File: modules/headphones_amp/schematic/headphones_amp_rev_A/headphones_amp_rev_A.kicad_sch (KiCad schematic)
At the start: 94 parts, among them J1 AudioJack3_SwitchTR, J2 AudioJack3_SwitchTR, Q1 BC140, Q10 BC548, Q11 BC548, Q12 BC140, Q13 BC160, Q14 BC548, Q15 BC557, Q16 BC548, Q2 BC160, Q3 BC548, Q4 BC557, Q5 BC548, Q6 BC548, Q7 BC548, Q8 BC557, Q9 BC557, SW1 SW_SPDT, SW2 SW_SPDT

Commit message: added draft footprint for the Wurth Connector
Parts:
- added C11, C12: 100pF, Capacitor_THT:C_Rect_L7.0mm_W2.0mm_P5.00mm, symbol Device:C
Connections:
- net at Q1.3 (C), R3.2: now also C11.2
- net at Q2.2 (B), Q5.1 (C), Q7.3 (E)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: now also C12.1
- net at Q2.3 (C), R4.1, R6.1: now also C12.2
- net at Q1.2 (B), Q7.1 (C), R14.1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: now also C11.1
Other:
- moved on the sheet: H1, H2, H3, H4

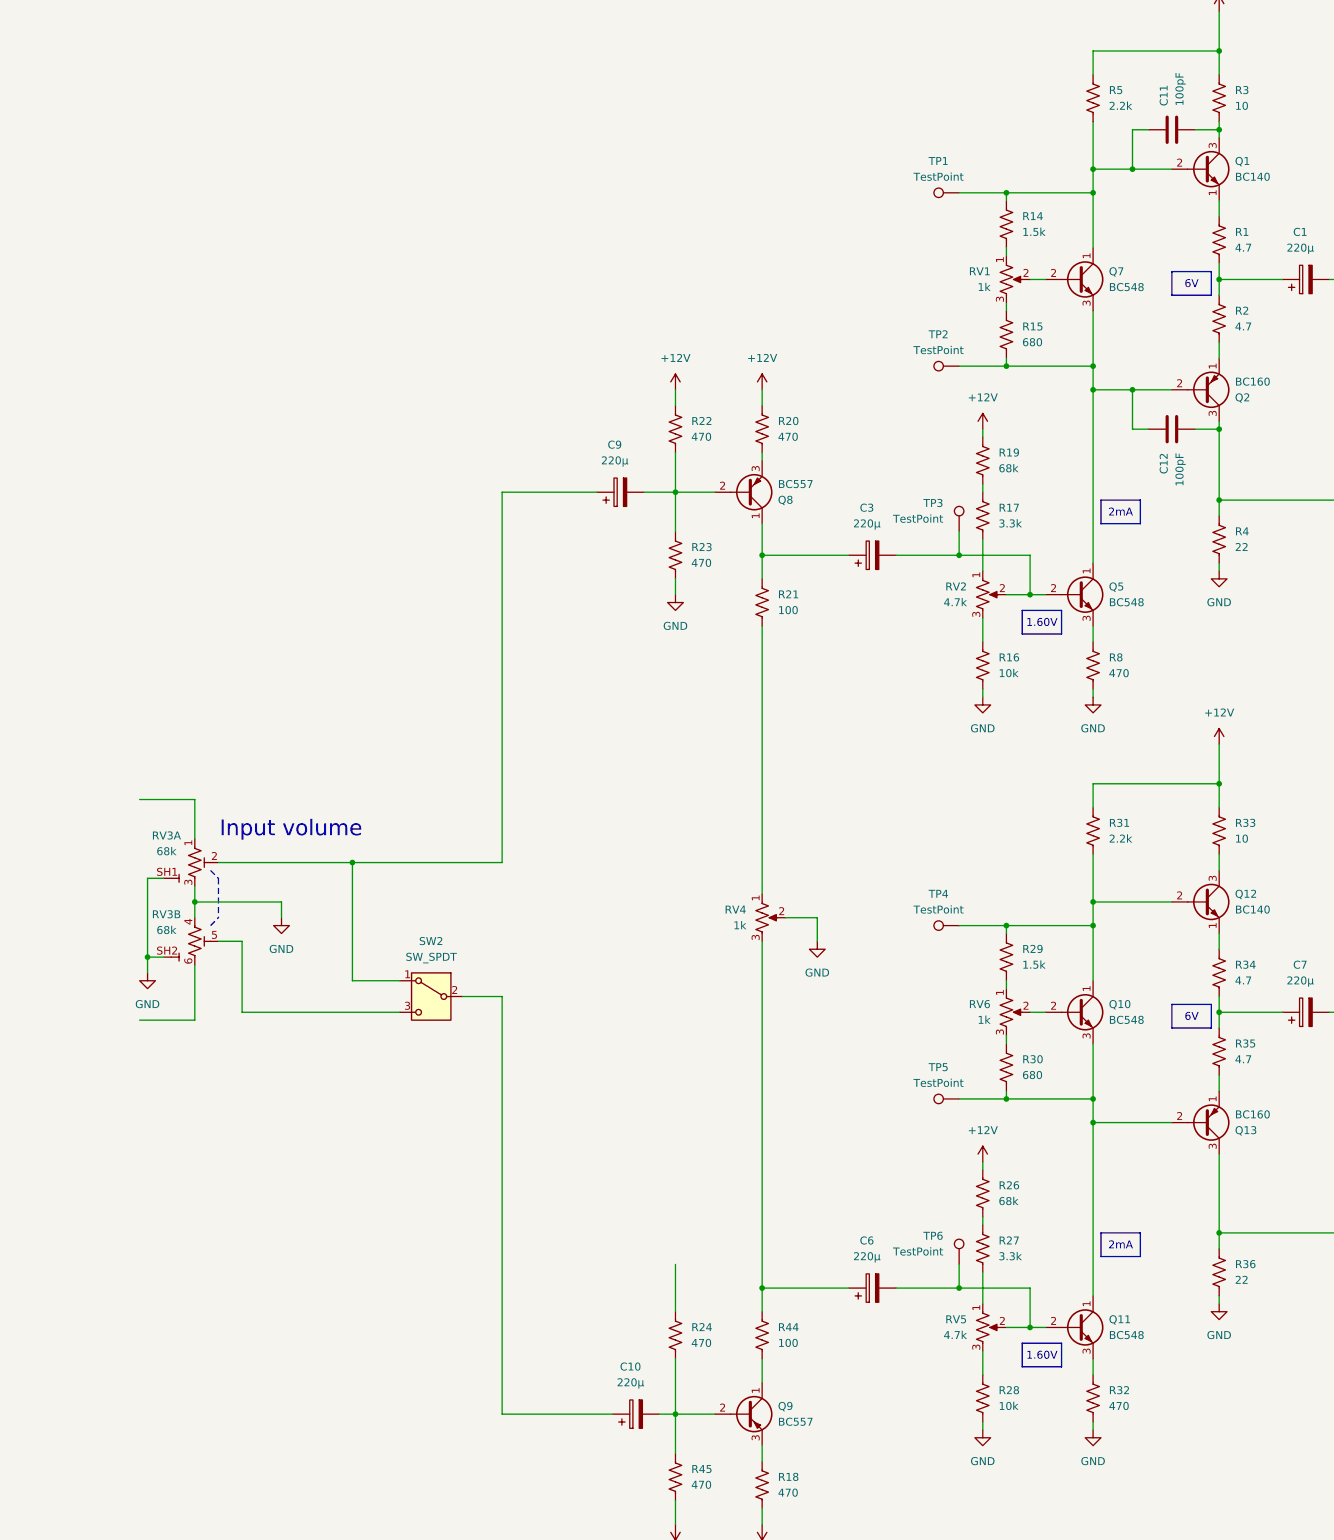
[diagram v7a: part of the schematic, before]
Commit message: attempt to fix wrong footprint
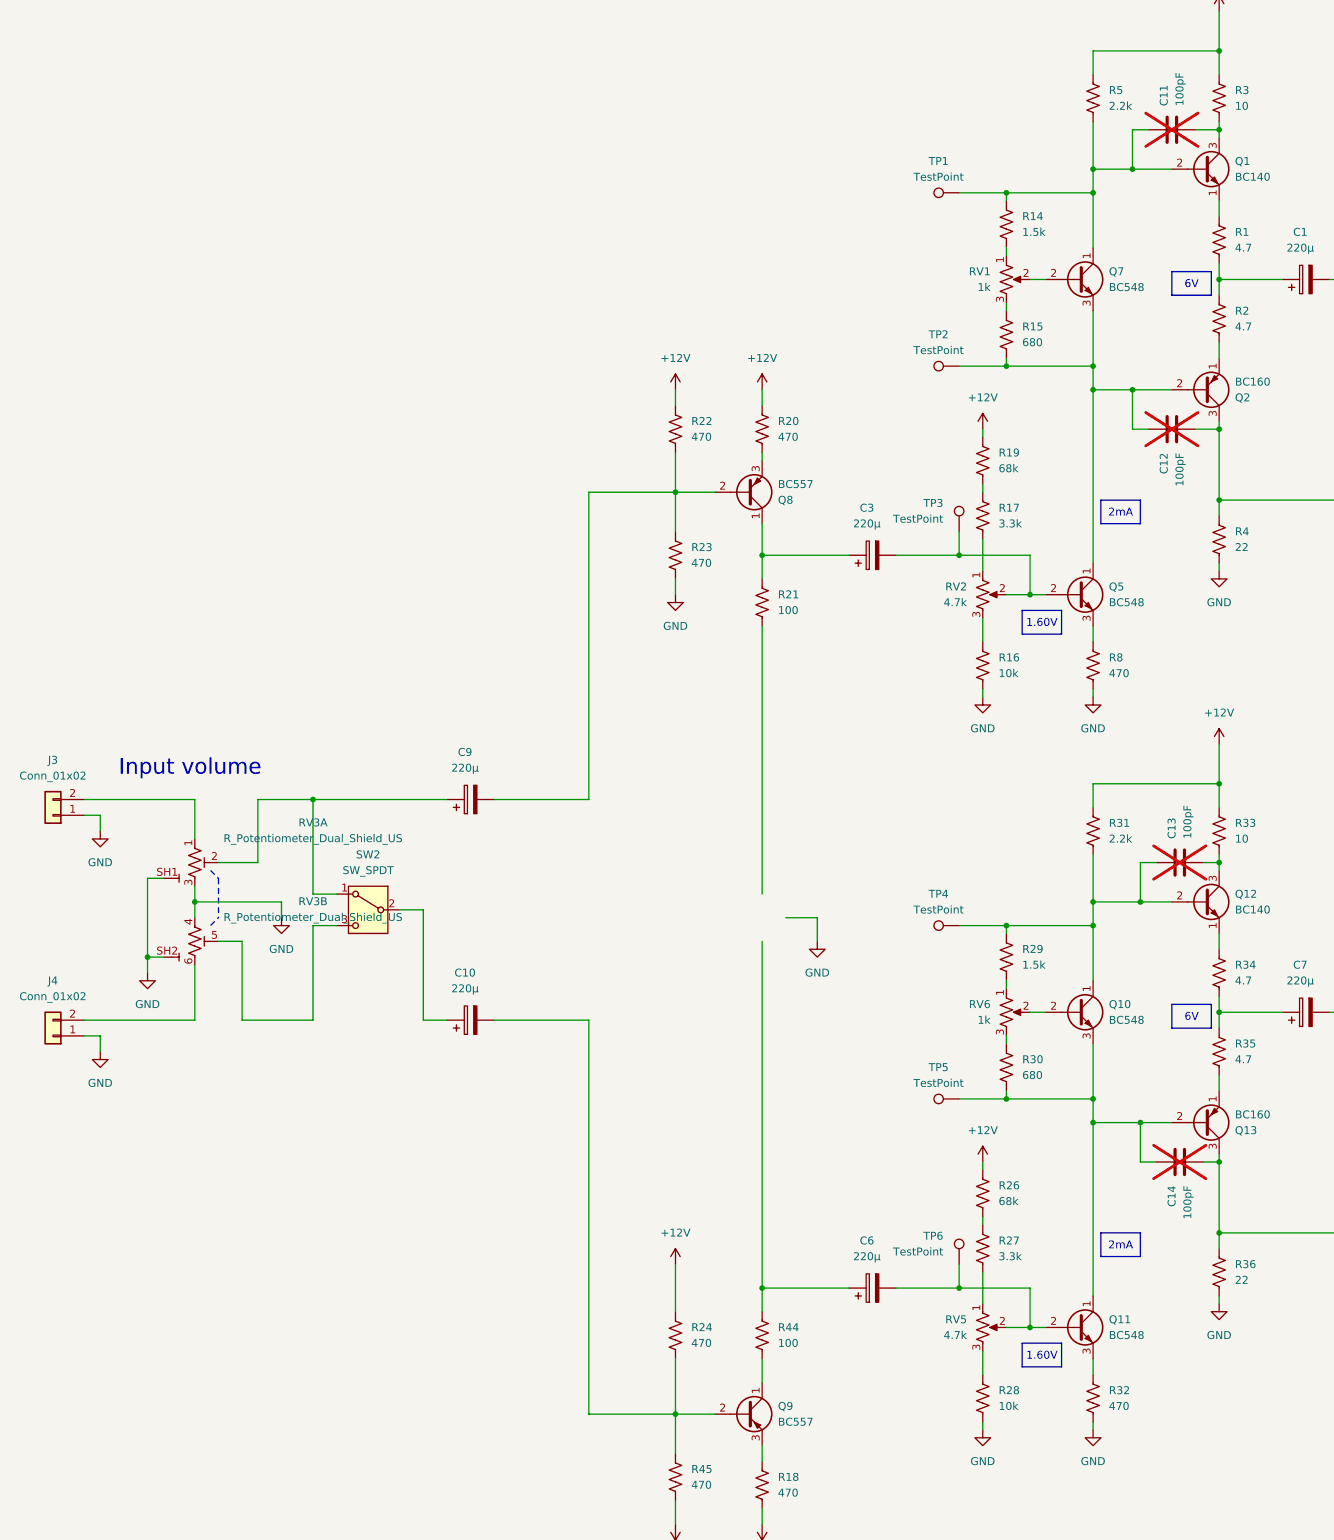
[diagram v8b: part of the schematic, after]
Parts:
- removed RV4: 1k, Potentiometer_THT:Potentiometer_Alpha_RD901F-40-00D_Single_Vertical_CircularHoles, symbol Device:R_Potentiometer_US
- added C13, C14: 100pF, Capacitor_THT:C_Rect_L7.0mm_W2.0mm_P5.00mm, symbol Device:C
- added J3, J4: Conn_01x02, ProjectLib_Transient:WuerthElectronik_WR_TBL_Series_2109_1x02_P2.54mm_Horizontal, symbol Connector_Generic:Conn_01x02
- C11, C12: now not fitted
- RV3: value 68k -> R_Potentiometer_Dual_Shield_US
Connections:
- net +12V: now also R24.1
- net GND: now also J3.1 (Pin_1), J4.1 (Pin_1)
- net at RV3.6: now also J4.2 (Pin_2)
- net at Q10.3 (E), Q11.1 (C), Q13.2 (B)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: now also C14.1
- net at Q10.1 (C), Q12.2 (B), R29.1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: now also C13.1
- net at Q12.3 (C), R33.2: now also C13.2
- net at Q13.3 (C), R36.1, R37.1: now also C14.2
- net at RV3.1: now also J3.2 (Pin_2)
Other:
- moved on the sheet: C10, C9, SW2
